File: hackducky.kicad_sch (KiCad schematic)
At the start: 50 parts, among them J1 USB_A, J2 Conn_01x06_Pin, J3 Micro_SD_Card, J4 Conn_01x06_Pin, P2 USB_C_Plug, SW2 SW_DIP_x04, SW3 bootsel, SW4 SW_Push, U1 W25Q16JVSS, U2 AP2112K-3.3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

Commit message: schm full done
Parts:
- added BZ1: Buzzer, Buzzer_Beeper:Buzzer_CUI_CPT-9019S-SMT, symbol Device:Buzzer
- added J5: Conn_01x03_Pin, Connector_PinSocket_2.54mm:PinSocket_1x03_P2.54mm_Vertical, symbol Connector:Conn_01x03_Pin
- SW2: footprint (none) -> Button_Switch_THT:SW_DIP_SPSTx04_Slide_6.7x11.72mm_W7.62mm_P2.54mm_LowProfile
- SW3: value bootsel -> BOOT_SEL
- SW4: value SW_Push -> Programming Button
- Y1: footprint Crystal:Crystal_SMD_1210-4Pin_1.2x1.0mm -> Crystal:Crystal_SMD_Abracon_ABM8G-4Pin_3.2x2.5mm
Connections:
- net GND: now also SW4.1, BZ1.2 (-)
- net GPIO21: now also BZ1.1 (+)
- net GPIO22: now also J5.1 (Pin_1)
- net GPIO23: now also J5.2 (Pin_2)
- net GPIO24: now also J5.3 (Pin_3)
- net PUSH: no longer SW4.1
- net CLK renamed SD_CLK
- net CS renamed SD_CS
- net MISO renamed SD_MISO
- net MOSI renamed SD_MOSI
- no-connect marks 20 -> 15
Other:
- note added: "BOOT_SEL BUTTON"
- note removed: "bsel"
- moved on the sheet: R16, R17, R18, R19, R20, R21

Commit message: did pcb a lil bit
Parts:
- removed BZ1: Buzzer, Buzzer_Beeper:Buzzer_CUI_CPT-9019S-SMT, symbol Device:Buzzer
- removed J5: Conn_01x03_Pin, Connector_PinSocket_2.54mm:PinSocket_1x03_P2.54mm_Vertical, symbol Connector:Conn_01x03_Pin
- removed SW4: Programming Button, Button_Switch_THT:SW_PUSH_6mm, symbol Switch:SW_Push
- added J6: Conn_01x04_Pin, Connector_PinHeader_2.54mm:PinHeader_1x04_P2.54mm_Vertical, symbol Connector:Conn_01x04_Pin
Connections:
- net GPIO21: now also J6.1 (Pin_1)
- net GPIO22: now also J6.2 (Pin_2)
- net GPIO23: now also J6.3 (Pin_3)
- net GPIO24: now also J6.4 (Pin_4)

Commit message: did pcb most of work done wooo
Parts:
- removed J2, J4: Conn_01x06_Pin, Connector_PinSocket_2.54mm:PinSocket_1x06_P2.54mm_Vertical, symbol Connector:Conn_01x06_Pin
- removed J6: Conn_01x04_Pin, Connector_PinHeader_2.54mm:PinHeader_1x04_P2.54mm_Vertical, symbol Connector:Conn_01x04_Pin
- added J2: Conn_02x02_Top_Bottom, Connector_PinHeader_1.00mm:PinHeader_2x02_P1.00mm_Vertical_SMD, symbol Connector_Generic:Conn_02x02_Top_Bottom
- added R9: 1k, Resistor_SMD:R_0402_1005Metric, symbol Device:R
- C15: footprint Capacitor_SMD:C_0402_1005Metric -> Capacitor_SMD:C_0805_2012Metric
- R4, R5: footprint Resistor_SMD:R_0805_2012Metric -> Capacitor_SMD:C_0402_1005Metric
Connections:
- net GPIO21: now also J2.4 (Pin_4)
- net GPIO22: now also J2.2 (Pin_2)
- net GPIO23: now also J2.1 (Pin_1)
- net GPIO24: now also J2.3 (Pin_3)
- net XOUT: now also R9.1; no longer C12.1, Y1.3
- new net: C12.1, R9.2, Y1.3
- no-connect marks 15 -> 27

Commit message: full done yayayay
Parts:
- removed D5, D6, D7: WS2812B, LED_SMD:LED_WS2812B-2020_PLCC4_2.0x2.0mm, symbol LED:SK6812
- removed SW2: SW_DIP_x04, Button_Switch_THT:SW_DIP_SPSTx04_Slide_6.7x11.72mm_W7.62mm_P2.54mm_LowProfile, symbol Switch:SW_DIP_x04
- added SW4: BOOT_SEL, Button_Switch_SMD:SW_Push_SPST_NO_Alps_SKRK, symbol Switch:SW_Push
- SW3: footprint Button_Switch_SMD:SW_Push_1P1T_XKB_TS-1187A -> Button_Switch_SMD:SW_Push_SPST_NO_Alps_SKRK
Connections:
- net GND: now also SW4.1
- net GPIO0: now also SW4.2
- net GPIO11: now also D4.2 (DIN)
- net GPIO17: no longer D4.2 (DIN)
- no-connect marks 27 -> 22
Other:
- moved on the sheet: D4

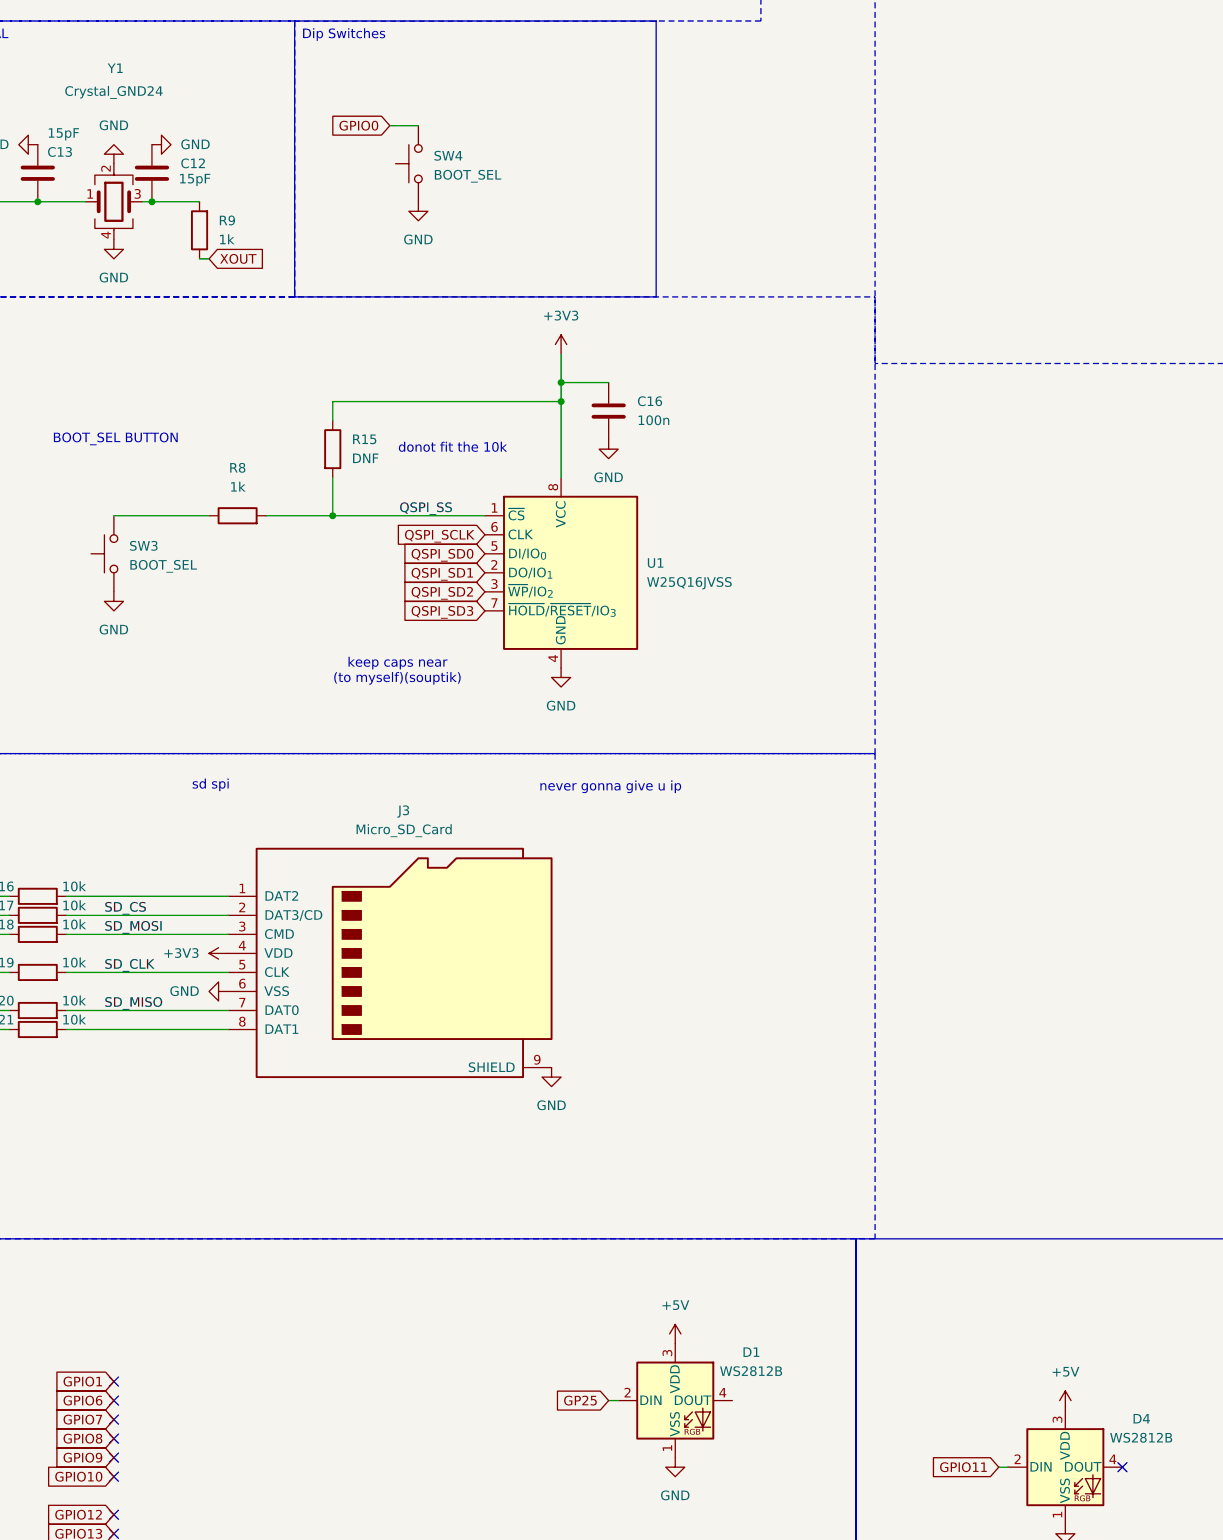
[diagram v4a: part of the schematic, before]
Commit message: v4 mostly tuned paths
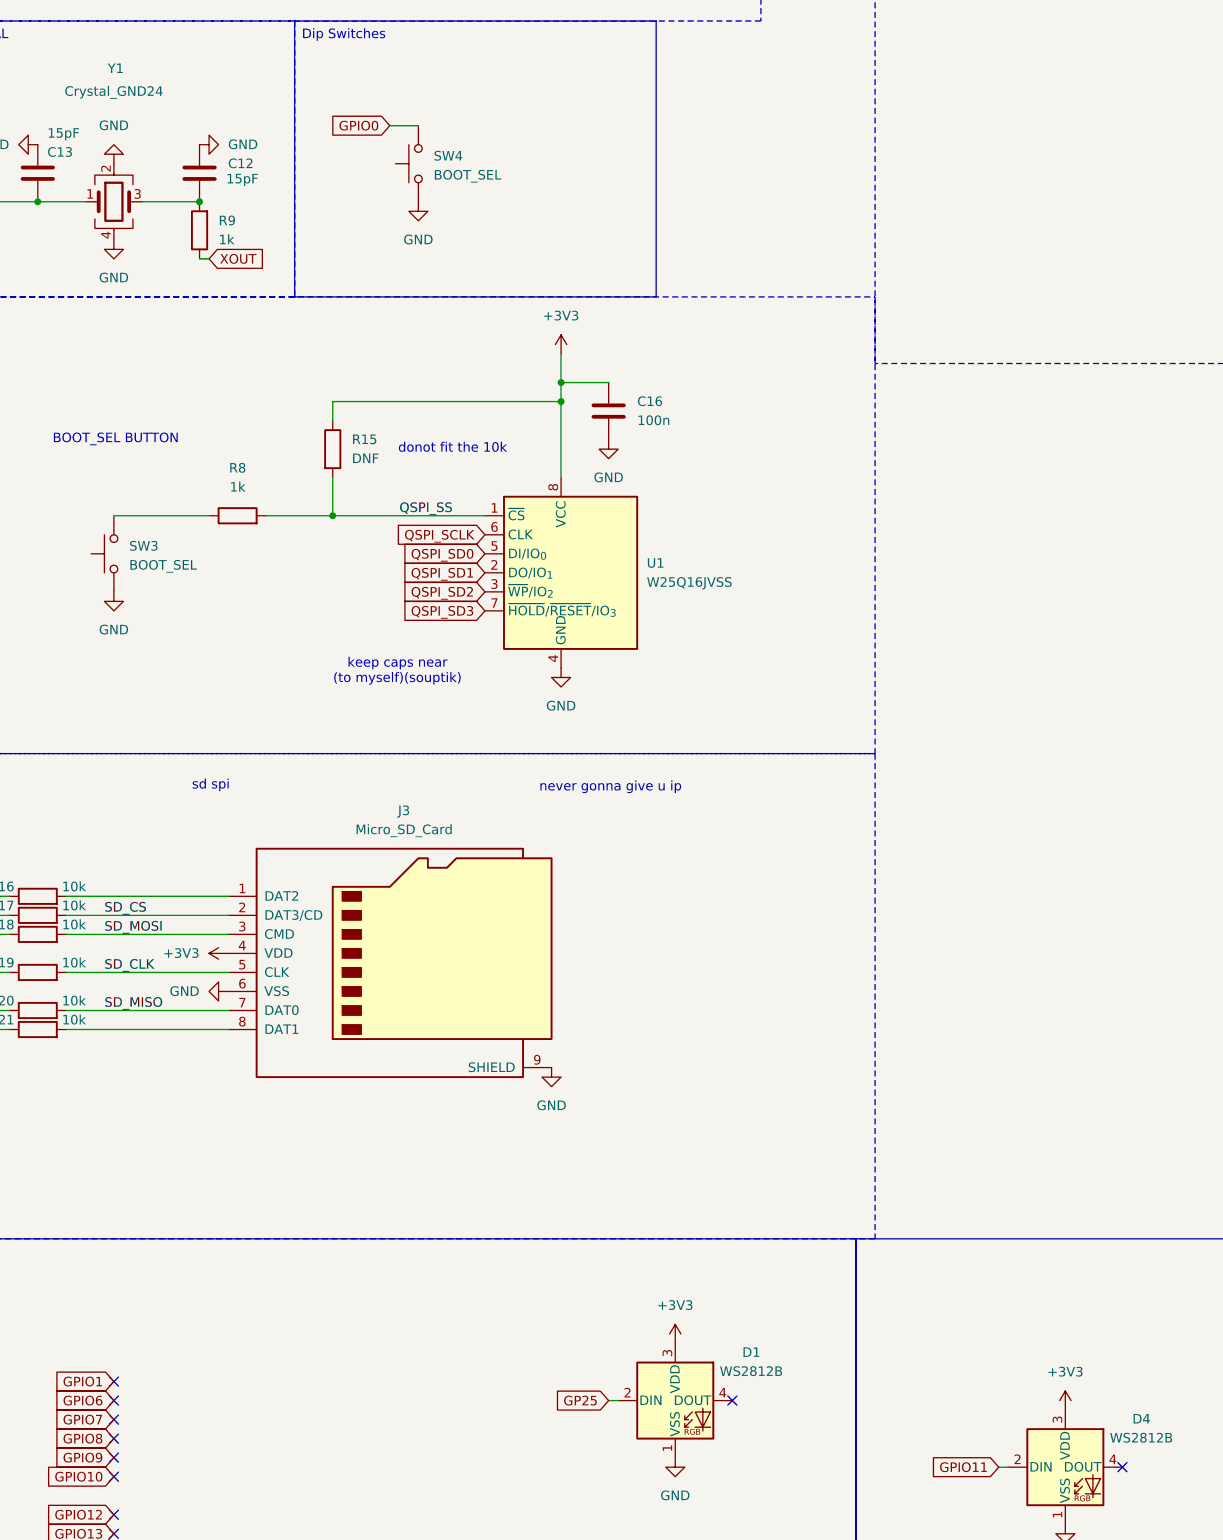
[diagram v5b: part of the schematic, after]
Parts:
- D1, D4: footprint LED_SMD:LED_WS2812B-2020_PLCC4_2.0x2.0mm -> LED_SMD:LED_SK6812_EC15_1.5x1.5mm
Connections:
- net +3V3: now also D1.3 (VDD), D4.3 (VDD)
- net +5V: no longer D1.3 (VDD), D4.3 (VDD)
- no-connect marks 22 -> 23
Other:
- moved on the sheet: C12
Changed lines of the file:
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@@
 	)
 	(junction
+		(at 46.99 172.72)
+		(diameter 0)
+		(color 0 0 0 0)
+	)
+	(junction
 		(at 255.27 72.39)
 		(diameter 0)
@@
 	)
 	(junction
-		(at 40.64 172.72)
-		(diameter 0)
-		(color 0 0 0 0)
-	)
-	(junction
 		(at 288.29 50.8)
 		(diameter 0)
@@
 	)
 	(no_connect
+		(at 118.11 332.74)
+	)
+	(no_connect
 		(at 48.26 128.27)
 	)
@@
 	(wire
 		(pts
-			(xy 39.37 172.72) (xy 40.64 172.72)
+			(xy 39.37 172.72) (xy 46.99 172.72)
 		)
 		(stroke
@@
 	(wire
 		(pts
-			(xy 46.99 172.72) (xy 40.64 172.72)
-		)
-		(stroke
-			(width 0)
-			(type default)
-		)
-	)
-	(wire
-		(pts
 			(xy 226.06 72.39) (xy 220.98 72.39)
 		)
@@
 			)
 		)
-		(property "Footprint" "LED_SMD:LED_WS2812B-2020_PLCC4_2.0x2.0mm"
+		(property "Footprint" "LED_SMD:LED_SK6812_EC15_1.5x1.5mm"
 			(at 111.76 340.36 0)
 			(effects
@@
 	(symbol
 		(lib_id "Device:C")
-		(at 40.64 168.91 180)
+		(at 46.99 168.91 180)
 		(unit 1)
 		(exclude_from_sim no)
@@
 		(dnp no)
 		(property "Reference" "C12"
-			(at 44.45 167.6399 0)
+			(at 50.8 167.6399 0)
 			(effects
 				(font
@@
 		)
 		(property "Value" "15pF"
-			(at 44.196 169.672 0)
+			(at 50.546 169.672 0)
 			(effects
 				(font
@@
 		)
 		(property "Footprint" "Capacitor_SMD:C_0402_1005Metric"
-			(at 39.6748 165.1 0)
+			(at 46.0248 165.1 0)
 			(effects
 				(font
@@
 		)
 		(property "Datasheet" "~"
-			(at 40.64 168.91 0)
+			(at 46.99 168.91 0)
 			(effects
 				(font
@@
 		)
 		(property "Description" "Unpolarized capacitor"
-			(at 40.64 168.91 0)
+			(at 46.99 168.91 0)
 			(effects
 				(font
@@
 			)
 		)
-		(property "Footprint" "LED_SMD:LED_WS2812B-2020_PLCC4_2.0x2.0mm"
+		(property "Footprint" "LED_SMD:LED_SK6812_EC15_1.5x1.5mm"
 			(at 163.83 349.25 0)
 			(effects
@@
 	)
 	(symbol
-		(lib_id "Device:C")
-		(at 104.14 34.29 270)
+		(lib_id "power:+3V3")
+		(at 110.49 325.12 0)
 		(unit 1)
 		(exclude_from_sim no)
@@
 		(dnp no)
 		(fields_autoplaced yes)
-		(property "Reference" "C15"
-			(at 104.14 26.67 90)
+		(property "Reference" "#PWR053"
+			(at 110.49 328.93 0)
 			(effects
 				(font
 					(size 1.27 1.27)
 				)
+				(hide yes)
 			)
 		)
-		(property "Value" "1uF"
-			(at 104.14 29.21 90)
+		(property "Value" "+3V3"
+			(at 110.49 320.04 0)
 			(effects
 				(font
@@
 			)
 		)
-		(property "Footprint" "Capacitor_SMD:C_0805_2012Metric"
-			(at 100.33 35.2552 0)
+		(property "Footprint" ""
+			(at 110.49 325.12 0)
 			(effects
 				(font
@@
 			)
 		)
-		(property "Datasheet" "~"
-			(at 104.14 34.29 0)
+		(property "Datasheet" ""
+			(at 110.49 325.12 0)
 			(effects
 				(font
@@
 			)
 		)
-		(property "Description" "Unpolarized capacitor"
-			(at 104.14 34.29 0)
+		(property "Description" "Power symbol creates a global label with name \"+3V3\""
+			(at 110.49 325.12 0)
 			(effects
 				(font
@@
 		(pin "1"
 		)
-		(pin "2"
-		)
 		(instances
-			(project "Hackducky"
+			(project "hackducky"
 				(path "/ac5af1a0-623d-4b6c-a3c0-6f81efb9cbcc"
-					(reference "C15")
+					(reference "#PWR053")
 					(unit 1)
 				)
@@
 	)
 	(symbol
-		(lib_id "power:+5V")
-		(at 110.49 325.12 0)
+		(lib_id "Device:C")
+		(at 104.14 34.29 270)
 		(unit 1)
 		(exclude_from_sim no)
@@
 		(dnp no)
 		(fields_autoplaced yes)
-		(property "Reference" "#PWR011"
-			(at 110.49 328.93 0)
+		(property "Reference" "C15"
+			(at 104.14 26.67 90)
 			(effects
 				(font
 					(size 1.27 1.27)
 				)
-				(hide yes)
 			)
 		)
-		(property "Value" "+5V"
-			(at 110.49 320.04 0)
+		(property "Value" "1uF"
+			(at 104.14 29.21 90)
 			(effects
 				(font
@@
 			)
 		)
-		(property "Footprint" ""
-			(at 110.49 325.12 0)
+		(property "Footprint" "Capacitor_SMD:C_0805_2012Metric"
+			(at 100.33 35.2552 0)
 			(effects
 				(font
@@
 			)
 		)
-		(property "Datasheet" ""
-			(at 110.49 325.12 0)
+		(property "Datasheet" "~"
+			(at 104.14 34.29 0)
 			(effects
 				(font
@@
 			)
 		)
-		(property "Description" "Power symbol creates a global label with name \"+5V\""
-			(at 110.49 325.12 0)
+		(property "Description" "Unpolarized capacitor"
+			(at 104.14 34.29 0)
 			(effects
 				(font
@@
 		(pin "1"
 		)
+		(pin "2"
+		)
 		(instances
-			(project ""
+			(project "Hackducky"
 				(path "/ac5af1a0-623d-4b6c-a3c0-6f81efb9cbcc"
-					(reference "#PWR011")
+					(reference "C15")
 					(unit 1)
 				)
@@
 	(symbol
 		(lib_id "power:+5V")
-		(at 162.56 334.01 0)
-		(unit 1)
-		(exclude_from_sim no)
-		(in_bom yes)
-		(on_board yes)
-		(dnp no)
-		(fields_autoplaced yes)
-		(property "Reference" "#PWR032"
-			(at 162.56 337.82 0)
-			(effects
-				(font
-					(size 1.27 1.27)
-				)
-				(hide yes)
-			)
-		)
-		(property "Value" "+5V"
-			(at 162.56 328.93 0)
-			(effects
-				(font
-					(size 1.27 1.27)
-				)
-			)
-		)
-		(property "Footprint" ""
-			(at 162.56 334.01 0)
-			(effects
-				(font
-					(size 1.27 1.27)
-				)
-				(hide yes)
-			)
-		)
-		(property "Datasheet" ""
-			(at 162.56 334.01 0)
-			(effects
-				(font
-					(size 1.27 1.27)
-				)
-				(hide yes)
-			)
-		)
-		(property "Description" "Power symbol creates a global label with name \"+5V\""
-			(at 162.56 334.01 0)
-			(effects
-				(font
-					(size 1.27 1.27)
-				)
-				(hide yes)
-			)
-		)
-		(pin "1"
-		)
-		(instances
-			(project "hackducky"
-				(path "/ac5af1a0-623d-4b6c-a3c0-6f81efb9cbcc"
-					(reference "#PWR032")
-					(unit 1)
-				)
-			)
-		)
-	)
-	(symbol
-		(lib_id "power:+5V")
 		(at 73.66 30.48 0)
 		(unit 1)
@@
 	(symbol
 		(lib_id "power:GND")
-		(at 40.64 165.1 90)
+		(at 46.99 165.1 90)
 		(unit 1)
 		(exclude_from_sim no)
@@
 		(fields_autoplaced yes)
 		(property "Reference" "#PWR017"
-			(at 46.99 165.1 0)
+			(at 53.34 165.1 0)
 			(effects
 				(font
@@
 		)
 		(property "Value" "GND"
-			(at 44.45 165.0999 90)
+			(at 50.8 165.0999 90)
 			(effects
 				(font
@@
 		)
 		(property "Footprint" ""
-			(at 40.64 165.1 0)
+			(at 46.99 165.1 0)
 			(effects
 				(font
@@
 		)
 		(property "Datasheet" ""
-			(at 40.64 165.1 0)
+			(at 46.99 165.1 0)
 			(effects
 				(font
@@
 		)
 		(property "Description" "Power symbol creates a global label with name \"GND\" , ground"
-			(at 40.64 165.1 0)
+			(at 46.99 165.1 0)
 			(effects
 				(font
@@
 					(unit 1)
 				)
+			)
+		)
+	)
+	(symbol
+		(lib_id "power:+3V3")
+		(at 162.56 334.01 0)
+		(unit 1)
+		(exclude_from_sim no)
+		(in_bom yes)
+		(on_board yes)
+		(dnp no)
+		(fields_autoplaced yes)
+		(property "Reference" "#PWR050"
+			(at 162.56 337.82 0)
+			(effects
+				(font
+					(size 1.27 1.27)
+				)
+				(hide yes)
+			)
+		)
+		(property "Value" "+3V3"
+			(at 162.56 328.93 0)
+			(effects
+				(font
+					(size 1.27 1.27)
+				)
+			)
+		)
+		(property "Footprint" ""
+			(at 162.56 334.01 0)
+			(effects
+				(font
+					(size 1.27 1.27)
+				)
+				(hide yes)
+			)
+		)
+		(property "Datasheet" ""
+			(at 162.56 334.01 0)
+			(effects
+				(font
+					(size 1.27 1.27)
+				)
+				(hide yes)
+			)
+		)
+		(property "Description" "Power symbol creates a global label with name \"+3V3\""
+			(at 162.56 334.01 0)
+			(effects
+				(font
+					(size 1.27 1.27)
+				)
+				(hide yes)
+			)
+		)
+		(pin "1"
+		)
+		(instances
+			(project "hackducky"
+				(path "/ac5af1a0-623d-4b6c-a3c0-6f81efb9cbcc"
+					(reference "#PWR050")
+					(unit 1)
+				)
